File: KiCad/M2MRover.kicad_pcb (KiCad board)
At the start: 2 copper layers, 80 x 90 mm, 48 parts, among them J1 microbit_edge_connector, J10 Ultrasonic Forward, J2 Left Motor, J3 Right Motor, J4 Serial (Bluetooth), J5 MPU6050 Gyro & Acc GY-521, J6 Compass GY-273, J7 Light Detection, J8 Servo, J9 Ultrasonic Down, U1 ESP8266-ESP-01, U2 L298HN, U3 LD1117V50, U4 LD1117V33

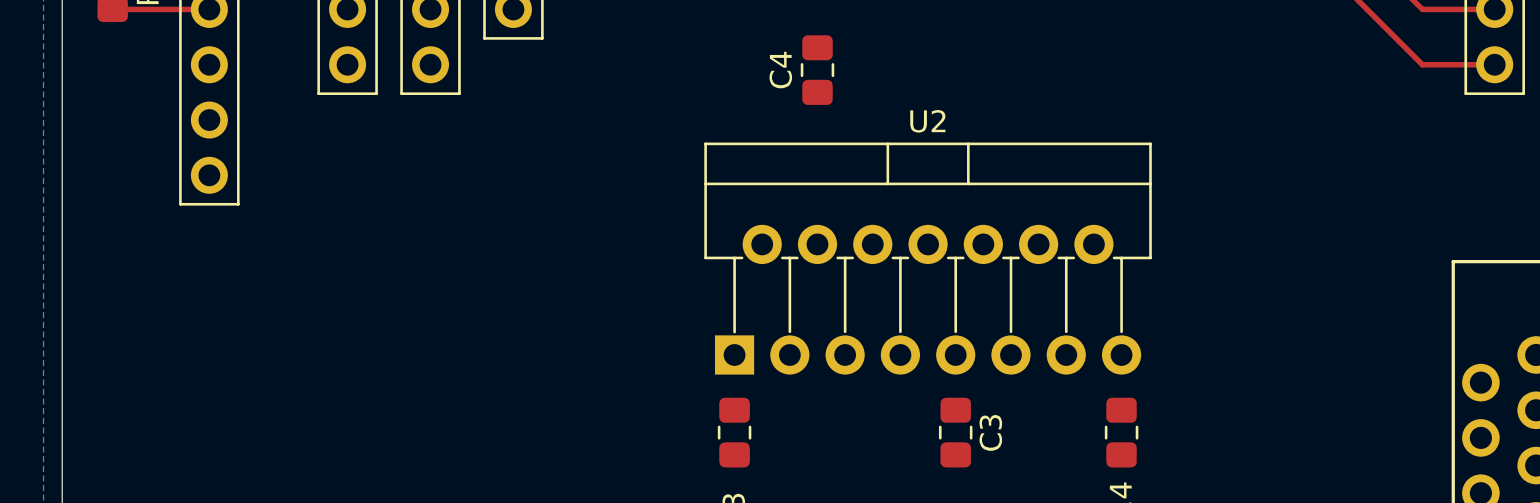
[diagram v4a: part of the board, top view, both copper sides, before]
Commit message: Add footprints for diodes
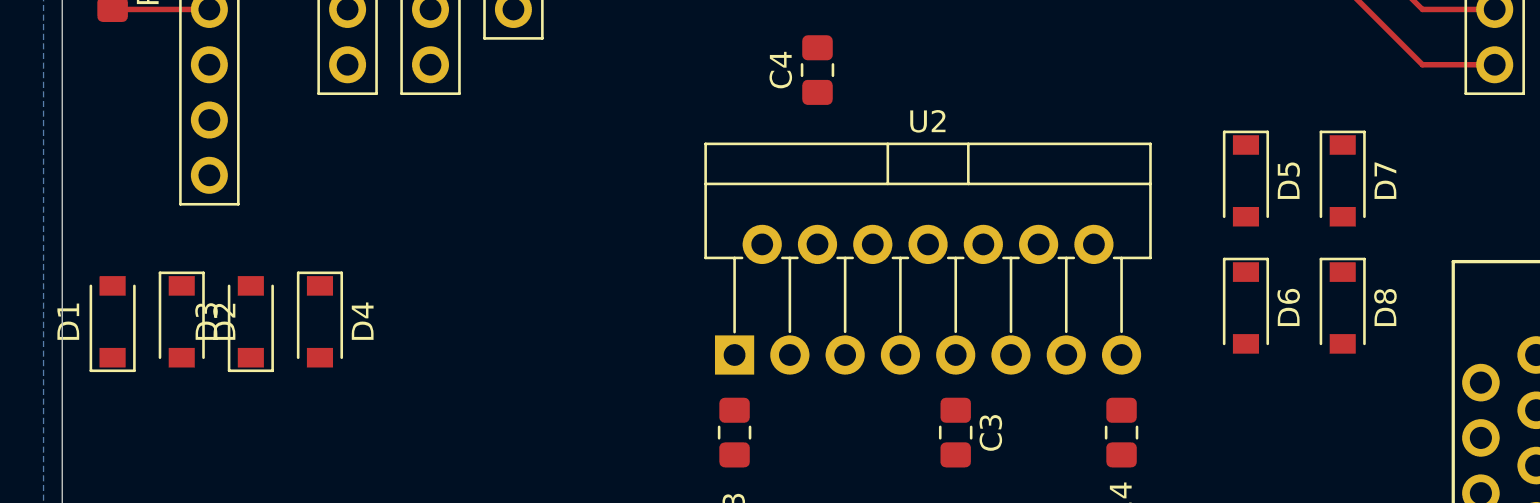
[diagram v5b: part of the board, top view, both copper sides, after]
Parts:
- added D1: 45V, 2A, Diode_SMD:D_SOD-123, F.Cu at (107.3, 67.7)
- added D2: 45V, 2A, Diode_SMD:D_SOD-123, F.Cu at (110.5, 67.7)
- added D3: 45V, 2A, Diode_SMD:D_SOD-123, F.Cu at (113.7, 67.7)
- added D4: 45V, 2A, Diode_SMD:D_SOD-123, F.Cu at (116.8, 67.7)
- added D5: 45V, 2A, Diode_SMD:D_SOD-123, F.Cu at (159.4, 61.2)
- added D6: 45V, 2A, Diode_SMD:D_SOD-123, F.Cu at (159.4, 67.1)
- added D7: 45V, 2A, Diode_SMD:D_SOD-123, F.Cu at (163.8, 61.2)
- added D8: 45V, 2A, Diode_SMD:D_SOD-123, F.Cu at (163.8, 67.1)

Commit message: Refactor motor wiring to h-bridge
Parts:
- moved R10 15.2 mm to (127.0, 92.5)
- moved R11 15.2 mm to (129.5, 92.5)
- moved R7 15.2 mm to (111.8, 92.5)
- moved R8 15.2 mm to (114.3, 92.5)
- moved R12 7.62 mm to (124.5, 92.5)
- moved R9 7.62 mm to (116.8, 92.5)
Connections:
- A1 pad 10: IN2 -> IN4
- A1 pad 11: IN1 -> IN3
- A1 pad 12: ENA -> ENB
- A1 pad 13: ENB -> ENA
- A1 pad 14: IN4 -> IN2
- A1 pad 15: IN3 -> IN1
- A1 pad 19: Right_LED -> Left_LED
- A1 pad 20: Left_LED -> Right_LED
- A1 pad 5: Left_Hall -> Right_Hall
- A1 pad 6: Right_Hall -> Left_Hall
- C1 pad 1: ENA -> ENB
- C2 pad 1: ENB -> ENA
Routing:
- net IN3: track 4.86 -> 47.3 mm
- net IN4: track 4.86 -> 44.9 mm, vias 0 -> 1
- net ENA: track 6.35 -> 46.2 mm
- net ENB: track 6.35 -> 44.4 mm
- net IN1: track 4.86 -> 41.4 mm
- net IN2: track 4.86 -> 40.3 mm
- net GND: track 44.8 -> 55.7 mm, vias 3 -> 8
- net +BATT: track 3.17 -> 10.2 mm
- net Net-(R14-Pad1): track 0.00 -> 2.54 mm
- net Net-(R13-Pad1): track 0.00 -> 2.54 mm
- net +5V: track 181.1 -> 183.7 mm

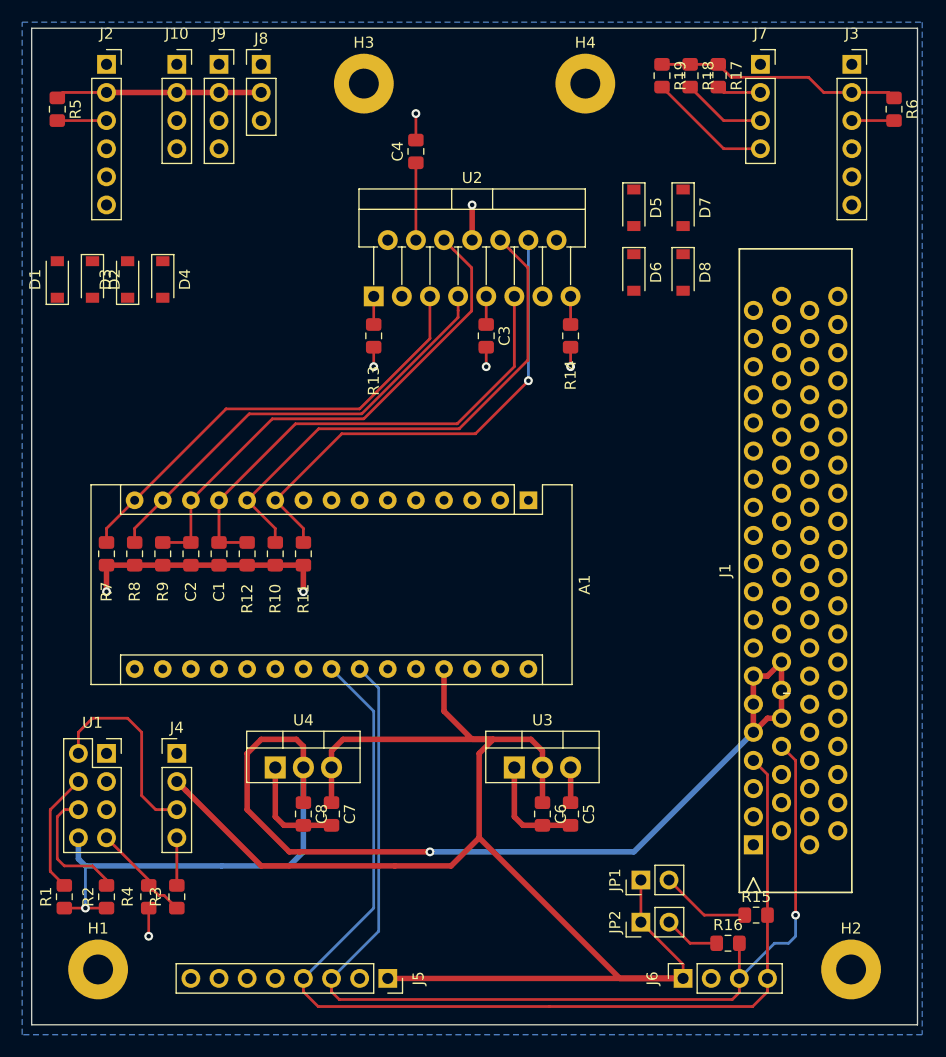
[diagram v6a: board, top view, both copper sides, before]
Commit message: Route the PCB
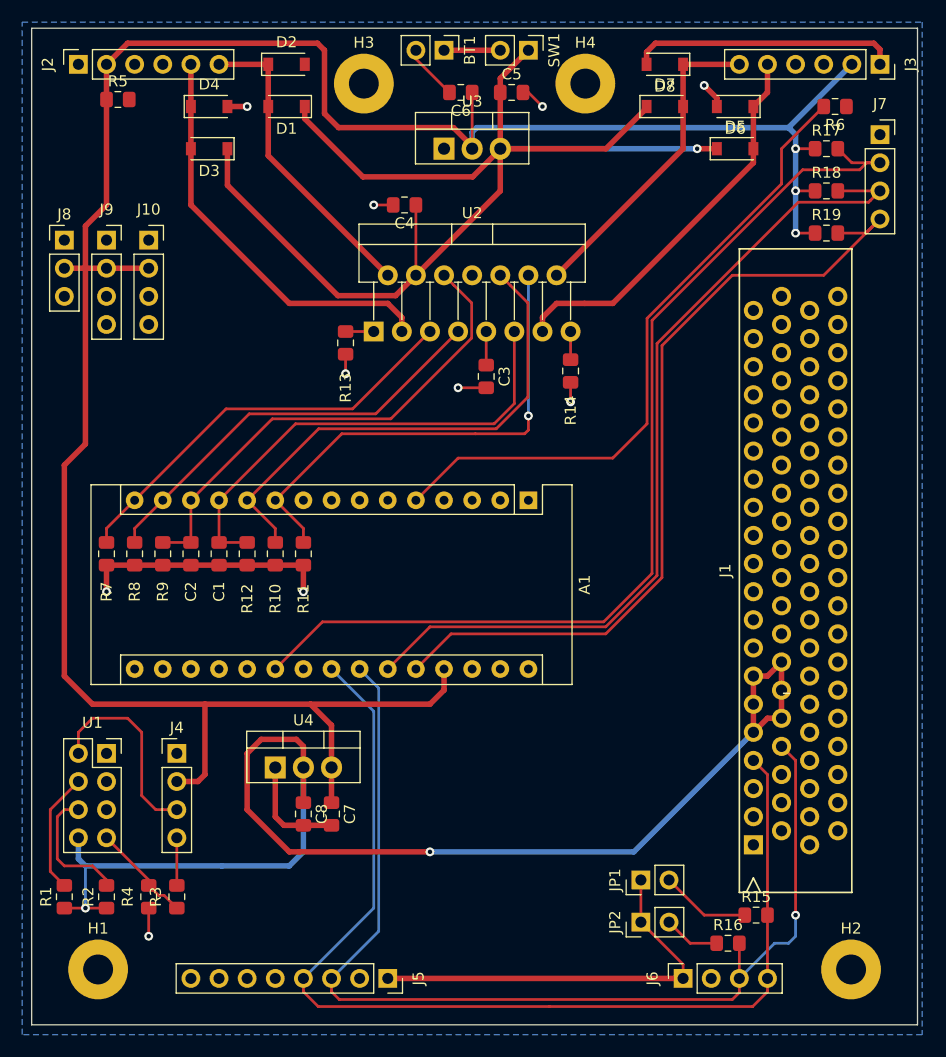
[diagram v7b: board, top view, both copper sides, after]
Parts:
- added BT1: Battery, Connector_PinHeader_2.54mm:PinHeader_1x02_P2.54mm_Vertical, F.Cu at (142.2, 47.0)
- added SW1: SW_SPST, Connector_PinHeader_2.54mm:PinHeader_1x02_P2.54mm_Vertical, F.Cu at (149.9, 47.0)
- moved C6 65.6 mm to (143.8, 50.8), turned to 180 degrees
- moved C5 65.4 mm to (148.3, 50.8), turned to 0 degrees
- moved U3 56.2 mm to (142.2, 55.9)
- moved D2 26.2 mm to (128.0, 48.3), turned to 0 degrees
- moved D1 25.9 mm to (128.0, 52.1), turned to 180 degrees
- moved J8 23.8 mm to (108.0, 64.1)
- moved R19 20.6 mm to (176.8, 63.5), turned to 0 degrees
- moved D8 18.9 mm to (162.2, 48.3), turned to 180 degrees
- moved J9 18.8 mm to (111.8, 64.1)
- moved D6 17.6 mm to (168.5, 52.1), turned to 180 degrees
- moved D4 16.2 mm to (121.0, 52.1), turned to 0 degrees
- moved R18 16.1 mm to (176.8, 59.7), turned to 0 degrees
- moved J10 16.1 mm to (115.6, 64.1)
- moved D3 13.9 mm to (121.0, 55.9), turned to 180 degrees
- moved J7 12.5 mm to (181.6, 54.6)
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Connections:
- J2 pad 5: OUT1 -> OUT2
- J2 pad 6: OUT2 -> OUT1
- J3 pad 5: OUT4 -> OUT3
- J3 pad 6: OUT3 -> OUT4
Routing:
- net +BATT: track 10.2 -> 112.5 mm, vias 0 -> 1
- net Right_LDR: track 4.01 -> 91.3 mm
- net +5V: track 183.7 -> 260.9 mm, vias 0 -> 3
- net Middle_LDR: track 7.61 -> 78.4 mm
- net Left_LDR: track 11.2 -> 75.4 mm
- net Right_Hall: track 3.81 -> 59.0 mm
- net OUT2: track 0.00 -> 37.2 mm
- net OUT3: track 0.00 -> 35.5 mm
- net OUT4: track 0.00 -> 28.9 mm
- net OUT1: track 0.00 -> 28.0 mm
- net GND: track 55.7 -> 78.4 mm, vias 8 -> 10
- net Net-(BT1-Pad1): track 0.00 -> 5.08 mm
- net Left_Hall: track 4.45 -> 0.00 mm
- net IN1: track 41.4 -> 37.8 mm
- net IN2: track 40.3 -> 37.8 mm
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
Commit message: Track everything apart from LEDs and MicroBit
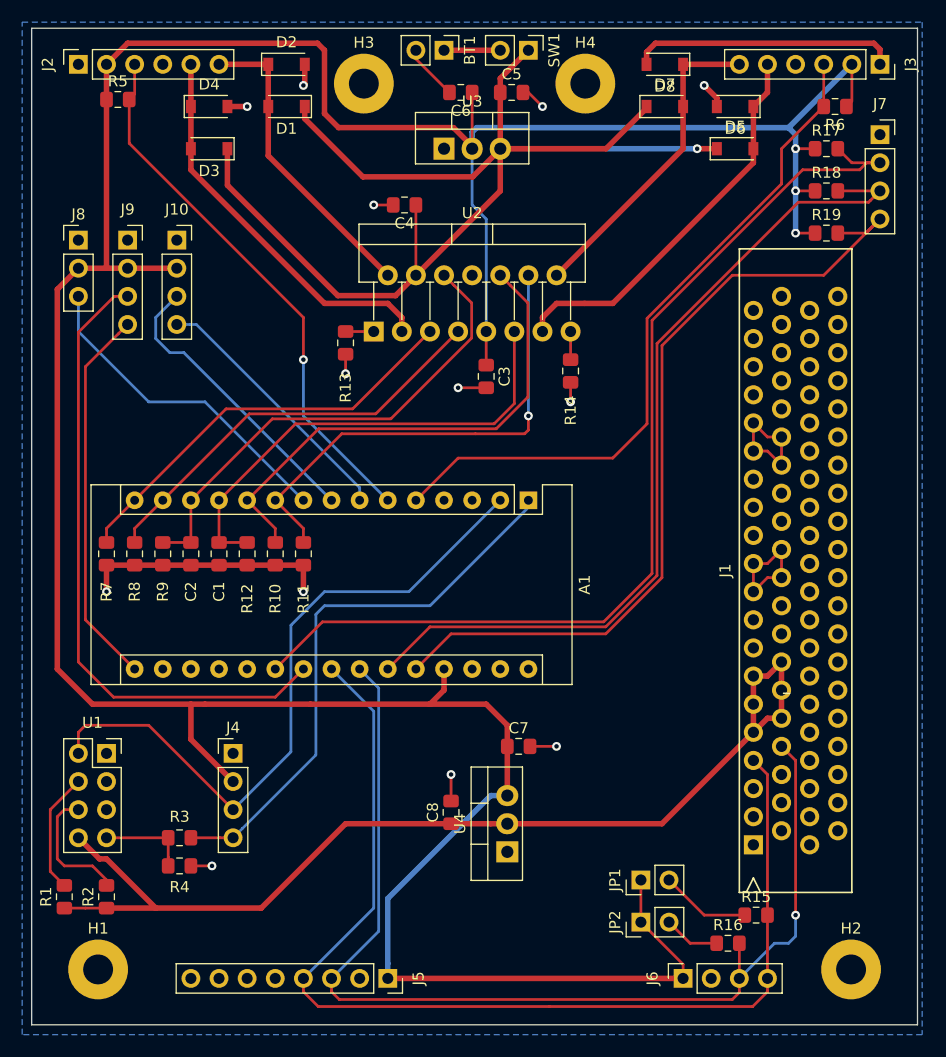
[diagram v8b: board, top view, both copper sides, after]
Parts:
- moved U4 22.3 mm to (148.0, 119.4), turned to 90 degrees
- moved C7 18.0 mm to (149.0, 109.9), turned to 0 degrees
- moved C8 13.3 mm to (142.9, 115.8), turned to 90 degrees
- moved R3 5.33 mm to (118.4, 118.1), turned to 180 degrees
- moved J4 5.08 mm to (123.2, 110.5)
- moved R4 3.94 mm to (118.4, 120.7), turned to 0 degrees
- moved J10 2.54 mm to (118.1, 64.1)
- moved J9 1.91 mm to (113.7, 64.1)
- moved J8 1.27 mm to (109.2, 64.1)
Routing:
- net Ultrasonic_Down_Echo: track 0.00 -> 58.3 mm
- net Left_Hall: track 0.00 -> 49.2 mm, vias 0 -> 1
- net +5V: track 260.9 -> 308.4 mm
- net TX: track 4.30 -> 50.9 mm
- net RX: track 18.1 -> 61.7 mm
- net Ultrasonic_Down_Trigger: track 0.00 -> 34.5 mm
- net Servo: track 0.00 -> 29.8 mm
- net +3V3: track 122.3 -> 94.7 mm, vias 2 -> 0
- net Ultrasonic_Forward_Echo: track 0.00 -> 26.5 mm
- net Ultrasonic_Forward_Trigger: track 0.00 -> 23.7 mm
- net ENB: track 43.1 -> 54.4 mm
- net ENA: track 44.5 -> 55.7 mm
- net Right_Hall: track 59.0 -> 62.8 mm
- net GND: track 78.4 -> 74.6 mm, vias 10 -> 13
- net OUT2: track 37.2 -> 35.4 mm
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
